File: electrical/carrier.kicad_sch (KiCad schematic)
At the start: 30 parts

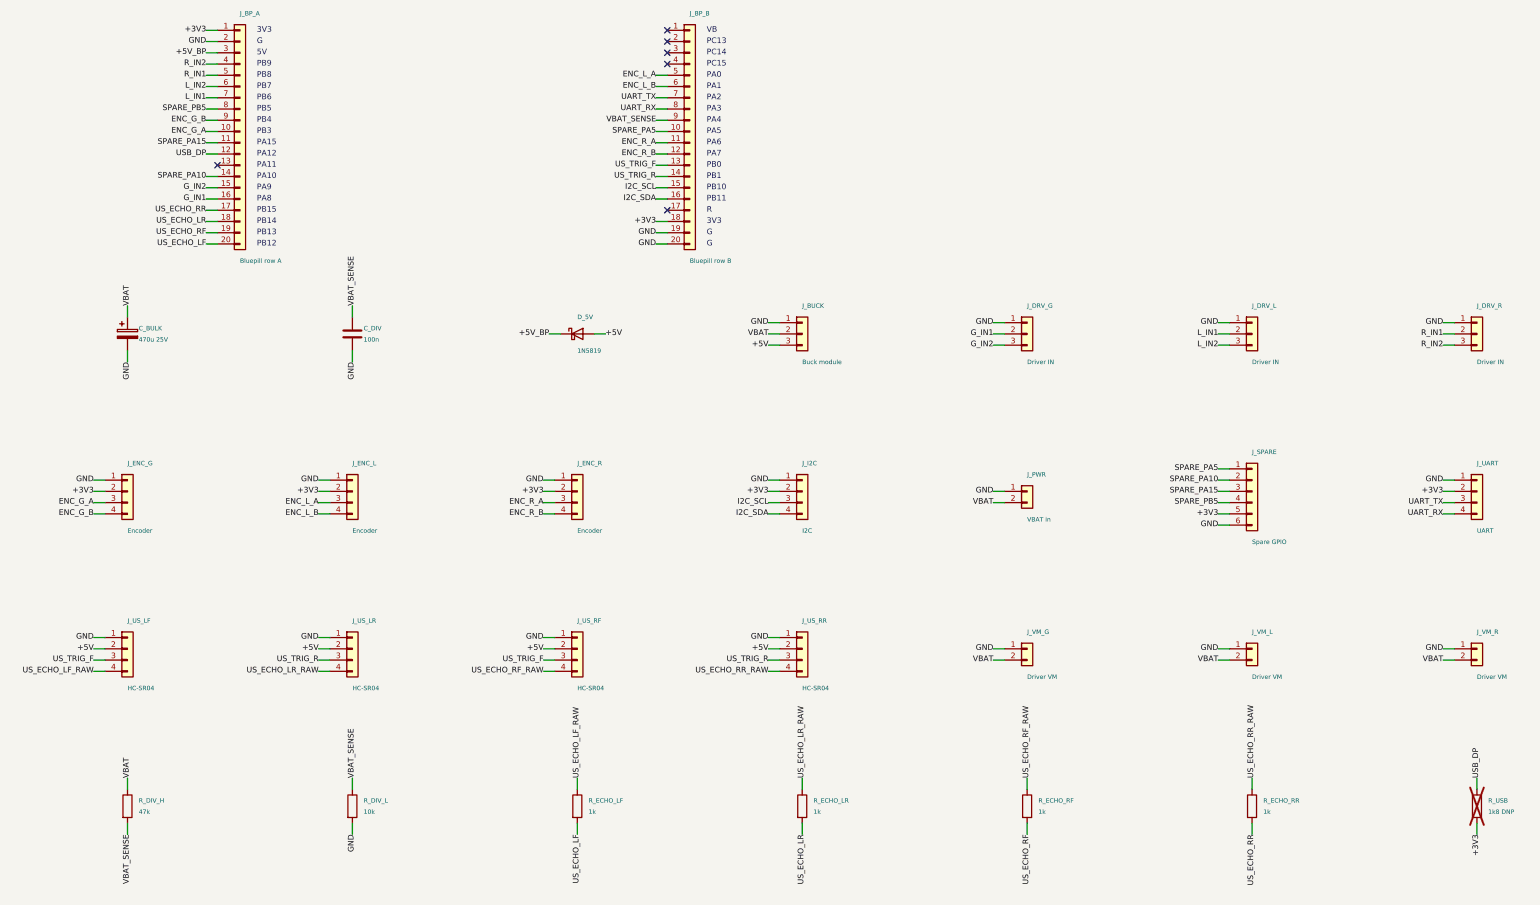
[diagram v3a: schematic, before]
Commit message: Regroup pins and connectors by side: 6 insulated wires instead of 34
Each Blue Pill row now serves its own side of the board: row B drives the
left motor (TIM2), left encoder (TIM3), left sonars and the battery
sense; row A drives the right motor and gripper (TIM4), right encoder
(TIM1) and right sonars. Every sonar gets its own trigger pin so no
signal crosses the board, and each connector sits beside its row in pin
order. Pins tied together on the Blue Pill (3V3, G) count as connected.
I2C and the spare header are dropped (PB10/PB11 now take echoes).

Perfboard: 6 insulated wires (from 34), 43 bare traces, 10 power wires.
Firmware, spec pin table and bring-up doc follow the new assignment.

Co-Authored-By: Claude Opus 5.5 <noreply@anthropic.com>
Claude-Session: https://claude.ai/code/session_01ENsByEFNd15FuMFFPy7PpL
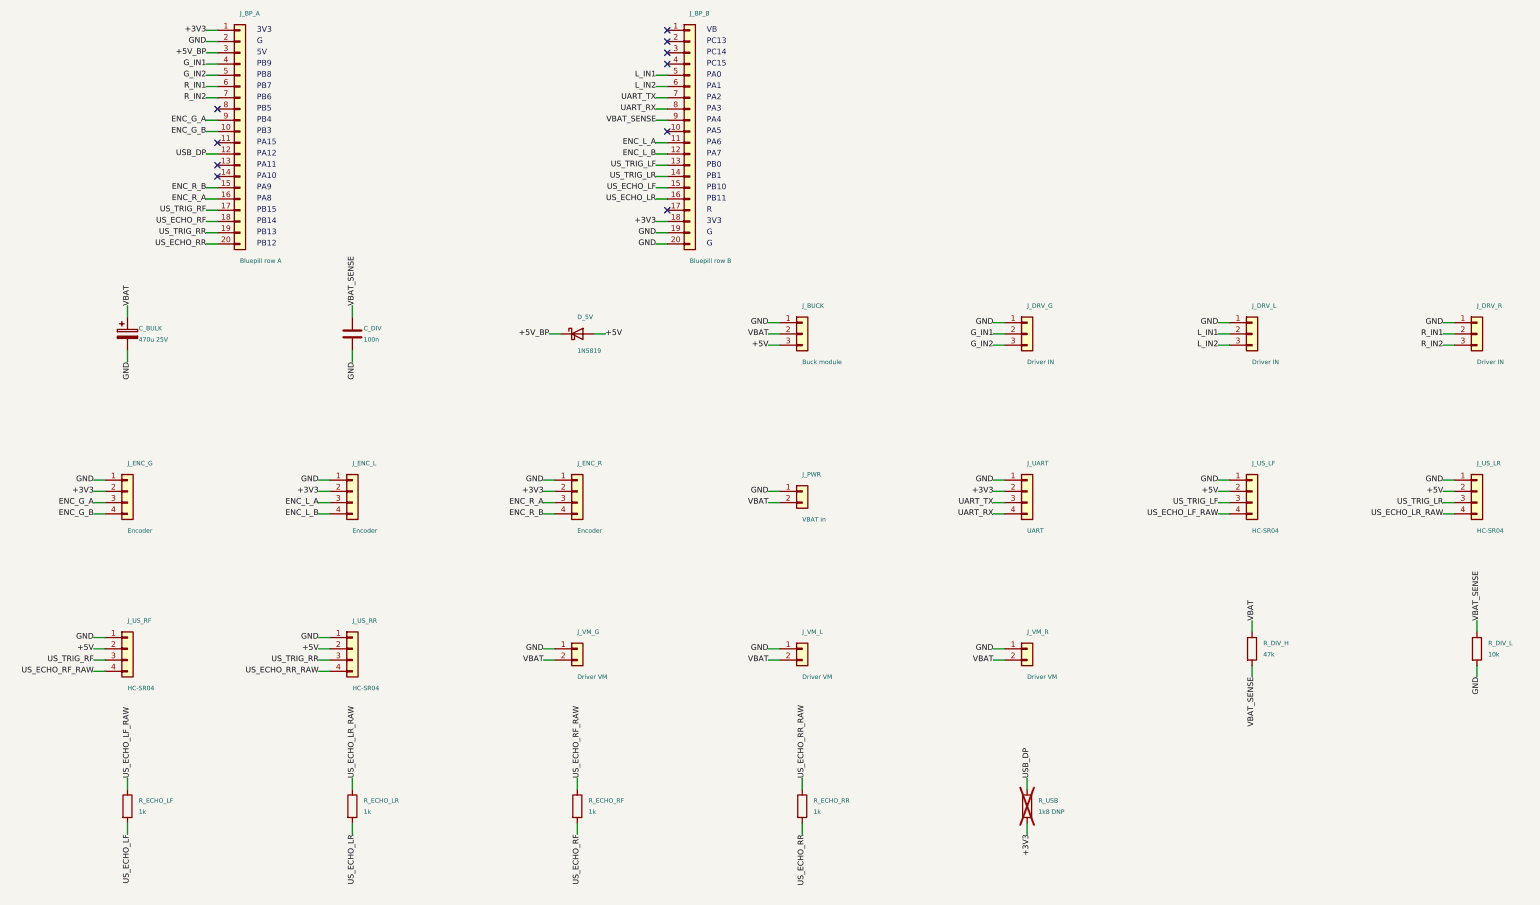
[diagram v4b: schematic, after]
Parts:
- removed J_I2C: I2C, Connector_JST:JST_XH_B4B-XH-A_1x04_P2.50mm_Vertical, symbol Connector_Generic:Conn_01x04
- removed J_SPARE: Spare GPIO, Connector_PinHeader_2.54mm:PinHeader_1x06_P2.54mm_Vertical, symbol Connector_Generic:Conn_01x06
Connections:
- net I2C_SCL is gone; now on net US_ECHO_LF: J_BP_B.15 (Pin_15)
- net I2C_SDA is gone; now on net US_ECHO_LR: J_BP_B.16 (Pin_16)
- net ENC_G_A: now also J_BP_A.9 (Pin_9); no longer J_BP_A.10 (Pin_10)
- net ENC_G_B: now also J_BP_A.10 (Pin_10); no longer J_BP_A.9 (Pin_9)
- net ENC_L_A: now also J_BP_B.11 (Pin_11); no longer J_BP_B.5 (Pin_5)
- net ENC_L_B: now also J_BP_B.12 (Pin_12); no longer J_BP_B.6 (Pin_6)
- net ENC_R_A: now also J_BP_A.16 (Pin_16); no longer J_BP_B.11 (Pin_11)
- net ENC_R_B: now also J_BP_A.15 (Pin_15); no longer J_BP_B.12 (Pin_12)
- net G_IN1: now also J_BP_A.4 (Pin_4); no longer J_BP_A.16 (Pin_16)
- net G_IN2: now also J_BP_A.5 (Pin_5); no longer J_BP_A.15 (Pin_15)
- net L_IN1: now also J_BP_B.5 (Pin_5); no longer J_BP_A.7 (Pin_7)
- net L_IN2: now also J_BP_B.6 (Pin_6); no longer J_BP_A.6 (Pin_6)
- net R_IN1: now also J_BP_A.6 (Pin_6); no longer J_BP_A.5 (Pin_5)
- net R_IN2: now also J_BP_A.7 (Pin_7); no longer J_BP_A.4 (Pin_4)
- net US_ECHO_LF: no longer J_BP_A.20 (Pin_20)
- net US_ECHO_LR: no longer J_BP_A.18 (Pin_18)
- net US_ECHO_RF: now also J_BP_A.18 (Pin_18); no longer J_BP_A.19 (Pin_19)
- net US_ECHO_RR: now also J_BP_A.20 (Pin_20); no longer J_BP_A.17 (Pin_17)
- net SPARE_PA10: no longer names the net of J_BP_A.14 (Pin_14)
- net SPARE_PA15: no longer names the net of J_BP_A.11 (Pin_11)
- net SPARE_PA5: no longer names the net of J_BP_B.10 (Pin_10)
- net SPARE_PB5: no longer names the net of J_BP_A.8 (Pin_8)
- net US_TRIG_F renamed US_TRIG_LF
- net US_TRIG_LF: no longer J_US_RF.3 (Pin_3)
- net US_TRIG_R renamed US_TRIG_LR
- net US_TRIG_LR: no longer J_US_RR.3 (Pin_3)
- new net US_TRIG_RF: J_BP_A.17 (Pin_17), J_US_RF.3 (Pin_3)
- new net US_TRIG_RR: J_BP_A.19 (Pin_19), J_US_RR.3 (Pin_3)
- no-connect marks 6 -> 10

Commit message: electrical: feed the drivers straight from the battery, not via the board
The DRV8871 modules take battery power on their own terminals, wired from
the branch after the e-stop. The board loses J_VM_L/G/R; its power input
now only feeds the buck module and the battery sense, so the AWG18 chain
shrinks to J_PWR, C_BULK and J_BUCK (4 wires instead of 10).

Co-Authored-By: Claude Opus 5.5 <noreply@anthropic.com>
Claude-Session: https://claude.ai/code/session_01ENsByEFNd15FuMFFPy7PpL
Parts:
- removed R_ECHO_RF, R_ECHO_RR: 1k, Resistor_THT:R_Axial_DIN0207_L6.3mm_D2.5mm_P10.16mm_Horizontal, symbol Device:R
- removed R_USB: 1k8 DNP, Resistor_THT:R_Axial_DIN0207_L6.3mm_D2.5mm_P10.16mm_Horizontal, symbol Device:R
- R_DIV_H: renamed from J_VM_G; value Driver VM -> 47k; footprint TerminalBlock_Phoenix:TerminalBlock_Phoenix_MKDS-1,5-2-5.08_1x02_P5.08mm_Horizontal -> Resistor_THT:R_Axial_DIN0207_L6.3mm_D2.5mm_P10.16mm_Horizontal; symbol Connector_Generic:Conn_01x02 -> Device:R
- R_DIV_L: renamed from J_VM_L; value Driver VM -> 10k; footprint TerminalBlock_Phoenix:TerminalBlock_Phoenix_MKDS-1,5-2-5.08_1x02_P5.08mm_Horizontal -> Resistor_THT:R_Axial_DIN0207_L6.3mm_D2.5mm_P10.16mm_Horizontal; symbol Connector_Generic:Conn_01x02 -> Device:R
- R_ECHO_LF: renamed from J_VM_R; value Driver VM -> 1k; footprint TerminalBlock_Phoenix:TerminalBlock_Phoenix_MKDS-1,5-2-5.08_1x02_P5.08mm_Horizontal -> Resistor_THT:R_Axial_DIN0207_L6.3mm_D2.5mm_P10.16mm_Horizontal; symbol Connector_Generic:Conn_01x02 -> Device:R
- R_ECHO_LR: renamed from R_DIV_H; value 47k -> 1k
- R_ECHO_RF: renamed from R_DIV_L; value 10k -> 1k
- R_USB: renamed from R_ECHO_LR; value 1k -> 1k8 DNP; now not fitted
- renumbered R_ECHO_LF to R_ECHO_RR
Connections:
- net +3V3: now also R_USB.2
- net GND: now also R_DIV_L.2; no longer R_DIV_H.1 (Pin_1), R_DIV_L.1 (Pin_1), R_ECHO_LF.1 (Pin_1), R_ECHO_RF.2
- net USB_DP: now also R_USB.1
- net US_ECHO_LF: now also R_ECHO_LF.2; no longer R_ECHO_RR.2
- net US_ECHO_LF_RAW: now also R_ECHO_LF.1; no longer R_ECHO_RR.1
- net US_ECHO_LR: now also R_ECHO_LR.2; no longer R_USB.2
- net US_ECHO_LR_RAW: now also R_ECHO_LR.1; no longer R_USB.1
- net US_ECHO_RF: now also R_ECHO_RF.2
- net US_ECHO_RF_RAW: now also R_ECHO_RF.1
- net US_ECHO_RR: now also R_ECHO_RR.2
- net US_ECHO_RR_RAW: now also R_ECHO_RR.1
- net VBAT: now also R_DIV_H.1; no longer R_DIV_H.2 (Pin_2), R_DIV_L.2 (Pin_2), R_ECHO_LF.2 (Pin_2), R_ECHO_LR.1
- net VBAT_SENSE: now also R_DIV_H.2, R_DIV_L.1; no longer R_ECHO_LR.2, R_ECHO_RF.1

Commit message: electrical: driver and sonar connectors follow the modules' pin order
J_DRV becomes XH 4P in the DRV8871 header order (GND, VM, IN1, IN2) with
VM left unconnected on the board, and J_US follows the HC-SR04 header
(Vcc, Trig, Echo, Gnd), so the cables run straight through. GND is the
first or last pin and stays on the board edge; unconnected connector pins
are now treated as pins by the router and the drawings.

Placement is provisional (14 insulated wires) until the encoder cable
order is known; the wire-count test says so and is to be tightened again.

Co-Authored-By: Claude Opus 5.5 <noreply@anthropic.com>
Claude-Session: https://claude.ai/code/session_01ENsByEFNd15FuMFFPy7PpL
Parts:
- removed J_DRV_L, J_DRV_R: Driver IN, Connector_JST:JST_XH_B3B-XH-A_1x03_P2.50mm_Vertical, symbol Connector_Generic:Conn_01x03
- added J_DRV_L, J_DRV_R: Driver IN, Connector_JST:JST_XH_B4B-XH-A_1x04_P2.50mm_Vertical, symbol Connector_Generic:Conn_01x04
- J_DRV_G: footprint Connector_JST:JST_XH_B3B-XH-A_1x03_P2.50mm_Vertical -> Connector_JST:JST_XH_B4B-XH-A_1x04_P2.50mm_Vertical; symbol Connector_Generic:Conn_01x03 -> Connector_Generic:Conn_01x04
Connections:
- net +5V: now also J_US_LF.1 (Pin_1), J_US_LR.1 (Pin_1), J_US_RF.1 (Pin_1), J_US_RR.1 (Pin_1); no longer J_US_LF.2 (Pin_2), J_US_LR.2 (Pin_2), J_US_RF.2 (Pin_2), J_US_RR.2 (Pin_2)
- net GND: now also J_US_LF.4 (Pin_4), J_US_LR.4 (Pin_4), J_US_RF.4 (Pin_4), J_US_RR.4 (Pin_4), J_DRV_L.1 (Pin_1), J_DRV_R.1 (Pin_1); no longer J_US_LF.1 (Pin_1), J_US_LR.1 (Pin_1), J_US_RF.1 (Pin_1), J_US_RR.1 (Pin_1)
- net G_IN1: now also J_DRV_G.3 (Pin_3); no longer J_DRV_G.2 (Pin_2)
- net G_IN2: now also J_DRV_G.4 (Pin_4); no longer J_DRV_G.3 (Pin_3)
- net L_IN1: now also J_DRV_L.3 (Pin_3)
- net L_IN2: now also J_DRV_L.4 (Pin_4)
- net R_IN1: now also J_DRV_R.3 (Pin_3)
- net R_IN2: now also J_DRV_R.4 (Pin_4)
- net US_ECHO_LF_RAW: now also J_US_LF.3 (Pin_3); no longer J_US_LF.4 (Pin_4)
- net US_ECHO_LR_RAW: now also J_US_LR.3 (Pin_3); no longer J_US_LR.4 (Pin_4)
- net US_ECHO_RF_RAW: now also J_US_RF.3 (Pin_3); no longer J_US_RF.4 (Pin_4)
- net US_ECHO_RR_RAW: now also J_US_RR.3 (Pin_3); no longer J_US_RR.4 (Pin_4)
- net US_TRIG_LF: now also J_US_LF.2 (Pin_2); no longer J_US_LF.3 (Pin_3)
- net US_TRIG_LR: now also J_US_LR.2 (Pin_2); no longer J_US_LR.3 (Pin_3)
- net US_TRIG_RF: now also J_US_RF.2 (Pin_2); no longer J_US_RF.3 (Pin_3)
- net US_TRIG_RR: now also J_US_RR.2 (Pin_2); no longer J_US_RR.3 (Pin_3)
- no-connect marks 10 -> 13
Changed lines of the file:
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@@
   (no_connect (at 160.02 33.02))
   (no_connect (at 160.02 35.56))
+  (no_connect (at 236.22 96.52))
+  (no_connect (at 287.02 96.52))
+  (no_connect (at 337.82 96.52))
   (wire (pts (xy 58.42 27.94) (xy 55.88 27.94))
     (stroke (width 0.0))
@@
     (stroke (width 0.0))
   )
-  (wire (pts (xy 236.22 96.52) (xy 233.68 96.52))
-    (stroke (width 0.0))
-  )
   (wire (pts (xy 236.22 99.06) (xy 233.68 99.06))
     (stroke (width 0.0))
   )
+  (wire (pts (xy 236.22 101.6) (xy 233.68 101.6))
+    (stroke (width 0.0))
+  )
   (wire (pts (xy 287.02 93.98) (xy 284.48 93.98))
     (stroke (width 0.0))
   )
-  (wire (pts (xy 287.02 96.52) (xy 284.48 96.52))
-    (stroke (width 0.0))
-  )
   (wire (pts (xy 287.02 99.06) (xy 284.48 99.06))
     (stroke (width 0.0))
   )
+  (wire (pts (xy 287.02 101.6) (xy 284.48 101.6))
+    (stroke (width 0.0))
+  )
   (wire (pts (xy 337.82 93.98) (xy 335.28 93.98))
     (stroke (width 0.0))
   )
-  (wire (pts (xy 337.82 96.52) (xy 335.28 96.52))
-    (stroke (width 0.0))
-  )
   (wire (pts (xy 337.82 99.06) (xy 335.28 99.06))
     (stroke (width 0.0))
   )
+  (wire (pts (xy 337.82 101.6) (xy 335.28 101.6))
+    (stroke (width 0.0))
+  )
   (wire (pts (xy 33.02 129.54) (xy 30.48 129.54))
     (stroke (width 0.0))
@@
     (effects (font (size 1.27 1.27)) (justify right))
   )
-  (label "G_IN1" (at 233.68 96.52 180)
-    (effects (font (size 1.27 1.27)) (justify right))
-  )
-  (label "G_IN2" (at 233.68 99.06 180)
+  (label "G_IN1" (at 233.68 99.06 180)
+    (effects (font (size 1.27 1.27)) (justify right))
+  )
+  (label "G_IN2" (at 233.68 101.6 180)
     (effects (font (size 1.27 1.27)) (justify right))
   )
@@
     (effects (font (size 1.27 1.27)) (justify right))
   )
-  (label "L_IN1" (at 284.48 96.52 180)
-    (effects (font (size 1.27 1.27)) (justify right))
-  )
-  (label "L_IN2" (at 284.48 99.06 180)
+  (label "L_IN1" (at 284.48 99.06 180)
+    (effects (font (size 1.27 1.27)) (justify right))
+  )
+  (label "L_IN2" (at 284.48 101.6 180)
     (effects (font (size 1.27 1.27)) (justify right))
   )
@@
     (effects (font (size 1.27 1.27)) (justify right))
   )
-  (label "R_IN1" (at 335.28 96.52 180)
-    (effects (font (size 1.27 1.27)) (justify right))
-  )
-  (label "R_IN2" (at 335.28 99.06 180)
+  (label "R_IN1" (at 335.28 99.06 180)
+    (effects (font (size 1.27 1.27)) (justify right))
+  )
+  (label "R_IN2" (at 335.28 101.6 180)
     (effects (font (size 1.27 1.27)) (justify right))
   )
@@
     (effects (font (size 1.27 1.27)) (justify right))
   )
-  (label "GND" (at 284.48 129.54 180)
-    (effects (font (size 1.27 1.27)) (justify right))
-  )
-  (label "+5V" (at 284.48 132.08 180)
-    (effects (font (size 1.27 1.27)) (justify right))
-  )
-  (label "US_TRIG_LF" (at 284.48 134.62 180)
-    (effects (font (size 1.27 1.27)) (justify right))
-  )
-  (label "US_ECHO_LF_RAW" (at 284.48 137.16 180)
-    (effects (font (size 1.27 1.27)) (justify right))
-  )
-  (label "GND" (at 335.28 129.54 180)
-    (effects (font (size 1.27 1.27)) (justify right))
-  )
-  (label "+5V" (at 335.28 132.08 180)
-    (effects (font (size 1.27 1.27)) (justify right))
-  )
-  (label "US_TRIG_LR" (at 335.28 134.62 180)
-    (effects (font (size 1.27 1.27)) (justify right))
-  )
-  (label "US_ECHO_LR_RAW" (at 335.28 137.16 180)
-    (effects (font (size 1.27 1.27)) (justify right))
-  )
-  (label "GND" (at 30.48 165.1 180)
-    (effects (font (size 1.27 1.27)) (justify right))
-  )
-  (label "+5V" (at 30.48 167.64 180)
-    (effects (font (size 1.27 1.27)) (justify right))
-  )
-  (label "US_TRIG_RF" (at 30.48 170.18 180)
-    (effects (font (size 1.27 1.27)) (justify right))
-  )
-  (label "US_ECHO_RF_RAW" (at 30.48 172.72 180)
-    (effects (font (size 1.27 1.27)) (justify right))
-  )
-  (label "GND" (at 81.28 165.1 180)
-    (effects (font (size 1.27 1.27)) (justify right))
-  )
-  (label "+5V" (at 81.28 167.64 180)
-    (effects (font (size 1.27 1.27)) (justify right))
-  )
-  (label "US_TRIG_RR" (at 81.28 170.18 180)
-    (effects (font (size 1.27 1.27)) (justify right))
-  )
-  (label "US_ECHO_RR_RAW" (at 81.28 172.72 180)
+  (label "+5V" (at 284.48 129.54 180)
+    (effects (font (size 1.27 1.27)) (justify right))
+  )
+  (label "US_TRIG_LF" (at 284.48 132.08 180)
+    (effects (font (size 1.27 1.27)) (justify right))
+  )
+  (label "US_ECHO_LF_RAW" (at 284.48 134.62 180)
+    (effects (font (size 1.27 1.27)) (justify right))
+  )
+  (label "GND" (at 284.48 137.16 180)
+    (effects (font (size 1.27 1.27)) (justify right))
+  )
+  (label "+5V" (at 335.28 129.54 180)
+    (effects (font (size 1.27 1.27)) (justify right))
+  )
+  (label "US_TRIG_LR" (at 335.28 132.08 180)
+    (effects (font (size 1.27 1.27)) (justify right))
+  )
+  (label "US_ECHO_LR_RAW" (at 335.28 134.62 180)
+    (effects (font (size 1.27 1.27)) (justify right))
+  )
+  (label "GND" (at 335.28 137.16 180)
+    (effects (font (size 1.27 1.27)) (justify right))
+  )
+  (label "+5V" (at 30.48 165.1 180)
+    (effects (font (size 1.27 1.27)) (justify right))
+  )
+  (label "US_TRIG_RF" (at 30.48 167.64 180)
+    (effects (font (size 1.27 1.27)) (justify right))
+  )
+  (label "US_ECHO_RF_RAW" (at 30.48 170.18 180)
+    (effects (font (size 1.27 1.27)) (justify right))
+  )
+  (label "GND" (at 30.48 172.72 180)
+    (effects (font (size 1.27 1.27)) (justify right))
+  )
+  (label "+5V" (at 81.28 165.1 180)
+    (effects (font (size 1.27 1.27)) (justify right))
+  )
+  (label "US_TRIG_RR" (at 81.28 167.64 180)
+    (effects (font (size 1.27 1.27)) (justify right))
+  )
+  (label "US_ECHO_RR_RAW" (at 81.28 170.18 180)
+    (effects (font (size 1.27 1.27)) (justify right))
+  )
+  (label "GND" (at 81.28 172.72 180)
     (effects (font (size 1.27 1.27)) (justify right))
   )
@@
     )
   )
-  (symbol (lib_id "Connector_Generic:Conn_01x03") (at 241.3 96.52 0) (unit 1)
+  (symbol (lib_id "Connector_Generic:Conn_01x04") (at 241.3 96.52 0) (unit 1)
     (in_bom yes) (on_board yes) (dnp no)
     (property "Reference" "J_DRV_G" (id 0) (at 241.3 90.17 0)
       (effects (font (size 1.0 1.0)) (justify left))
     )
-    (property "Value" "Driver IN" (id 1) (at 241.3 102.87 0)
-      (effects (font (size 1.0 1.0)) (justify left))
-    )
-    (property "Footprint" "Connector_JST:JST_XH_B3B-XH-A_1x03_P2.50mm_Vertical" (id 2) (at 241.3 96.52 0)
+    (property "Value" "Driver IN" (id 1) (at 241.3 105.41 0)
+      (effects (font (size 1.0 1.0)) (justify left))
+    )
+    (property "Footprint" "Connector_JST:JST_XH_B4B-XH-A_1x04_P2.50mm_Vertical" (id 2) (at 241.3 96.52 0)
       (effects (font (size 1.0 1.0)) hide)
     )
@@
     (pin "2")
     (pin "3")
+    (pin "4")
     (instances
       (project "carrier"
@@
     )
   )
-  (symbol (lib_id "Connector_Generic:Conn_01x03") (at 292.1 96.52 0) (unit 1)
+  (symbol (lib_id "Connector_Generic:Conn_01x04") (at 292.1 96.52 0) (unit 1)
     (in_bom yes) (on_board yes) (dnp no)
     (property "Reference" "J_DRV_L" (id 0) (at 292.1 90.17 0)
       (effects (font (size 1.0 1.0)) (justify left))
     )
-    (property "Value" "Driver IN" (id 1) (at 292.1 102.87 0)
-      (effects (font (size 1.0 1.0)) (justify left))
-    )
-    (property "Footprint" "Connector_JST:JST_XH_B3B-XH-A_1x03_P2.50mm_Vertical" (id 2) (at 292.1 96.52 0)
+    (property "Value" "Driver IN" (id 1) (at 292.1 105.41 0)
+      (effects (font (size 1.0 1.0)) (justify left))
+    )
+    (property "Footprint" "Connector_JST:JST_XH_B4B-XH-A_1x04_P2.50mm_Vertical" (id 2) (at 292.1 96.52 0)
       (effects (font (size 1.0 1.0)) hide)
     )
@@
     (pin "2")
     (pin "3")
+    (pin "4")
     (instances
       (project "carrier"
@@
     )
   )
-  (symbol (lib_id "Connector_Generic:Conn_01x03") (at 342.9 96.52 0) (unit 1)
+  (symbol (lib_id "Connector_Generic:Conn_01x04") (at 342.9 96.52 0) (unit 1)
     (in_bom yes) (on_board yes) (dnp no)
     (property "Reference" "J_DRV_R" (id 0) (at 342.9 90.17 0)
       (effects (font (size 1.0 1.0)) (justify left))
     )
-    (property "Value" "Driver IN" (id 1) (at 342.9 102.87 0)
-      (effects (font (size 1.0 1.0)) (justify left))
-    )
-    (property "Footprint" "Connector_JST:JST_XH_B3B-XH-A_1x03_P2.50mm_Vertical" (id 2) (at 342.9 96.52 0)
+    (property "Value" "Driver IN" (id 1) (at 342.9 105.41 0)
+      (effects (font (size 1.0 1.0)) (justify left))
+    )
+    (property "Footprint" "Connector_JST:JST_XH_B4B-XH-A_1x04_P2.50mm_Vertical" (id 2) (at 342.9 96.52 0)
       (effects (font (size 1.0 1.0)) hide)
     )
@@
     (pin "2")
     (pin "3")
+    (pin "4")
     (instances
       (project "carrier"
